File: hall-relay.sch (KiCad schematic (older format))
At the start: 10 parts, among them J1 Screw_Terminal_1x04, Q1 AO3400, U1 HT71xx, U2 Hall-A3212

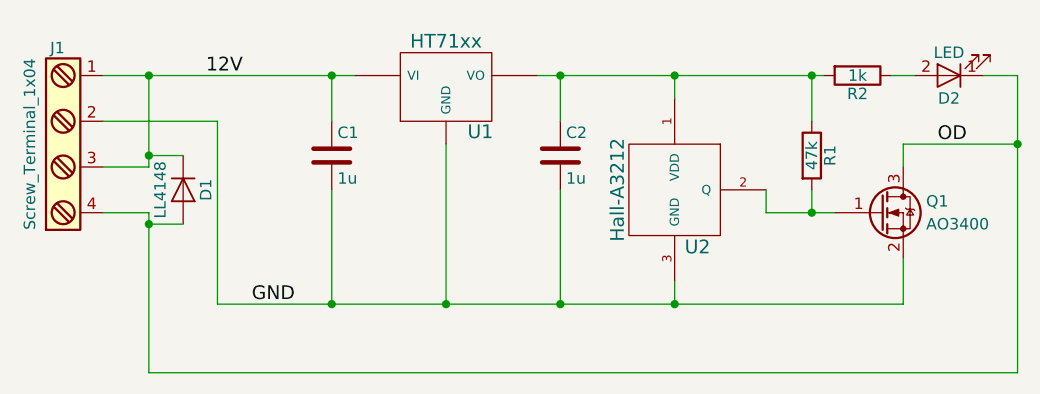
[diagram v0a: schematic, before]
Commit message: added LED pullup option to unregulated; avoids LED reverse-breakdown problems
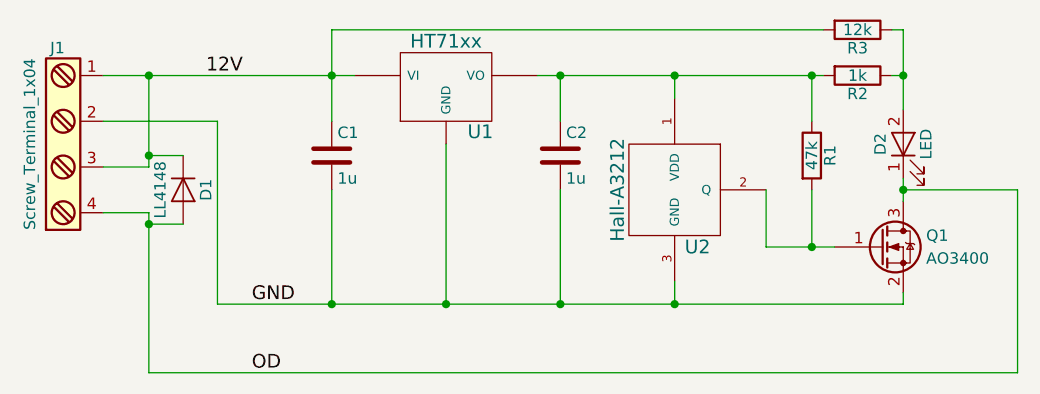
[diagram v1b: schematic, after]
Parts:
- added R3: 12k, Resistors_SMD:R_0805, symbol R
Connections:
- net 12V: now also R3.2
- net at D2.2 (A), R2.1: now also R3.1
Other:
- moved on the sheet: D2, Q1
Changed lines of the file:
@@
 	0    1    1    0
 $EndComp
-Text Label 6650 2200 0    60   ~ 0
-OD
 $Comp
 L Hall-A3212 U2
@@
 L Q_NMOS_GSD Q1
 U 1 1 5A364DBD
-P 6400 2500
-F 0 "Q1" H 6600 2550 50  0000 L CNN
-F 1 "AO3400" H 6600 2450 50  0000 L CNN
-F 2 "TO_SOT_Packages_SMD:SOT-23" H 6600 2600 50  0001 C CNN
-F 3 "" H 6400 2500 50  0000 C CNN
-	1    6400 2500
+P 6400 2650
+F 0 "Q1" H 6600 2700 50  0000 L CNN
+F 1 "AO3400" H 6600 2600 50  0000 L CNN
+F 2 "TO_SOT_Packages_SMD:SOT-23" H 6600 2750 50  0001 C CNN
+F 3 "" H 6400 2650 50  0000 C CNN
+	1    6400 2650
 	1    0    0    -1
 $EndComp
@@
 L LED D2
 U 1 1 5A366503
-P 6700 1900
-F 0 "D2" H 6700 2000 50  0000 C CNN
-F 1 "LED" H 6700 1800 50  0000 C CNN
-F 2 "LEDs:LED_0805" H 6700 1900 50  0001 C CNN
-F 3 "" H 6700 1900 50  0000 C CNN
-	1    6700 1900
-	-1   0    0    1
+P 6500 2200
+F 0 "D2" H 6500 2300 50  0000 C CNN
+F 1 "LED" H 6500 2100 50  0000 C CNN
+F 2 "LEDs:LED_0805" H 6500 2200 50  0001 C CNN
+F 3 "" H 6500 2200 50  0000 C CNN
+	1    6500 2200
+	0    -1   -1   0
 $EndComp
 $Comp
@@
 	3500 2100 3500 2900
 Wire Wire Line
-	6500 2900 6500 2700
-Wire Wire Line
 	4000 2400 4000 2900
 Connection ~ 4000 2900
@@
 	3200 2300 3200 1900
 Connection ~ 3200 1900
-Wire Wire Line
-	6500 2200 7000 2200
-Wire Wire Line
-	7000 1900 7000 3200
 Wire Wire Line
 	7000 3200 3200 3200
@@
 Connection ~ 5000 1900
 Wire Wire Line
-	6100 2400 6100 2500
-Wire Wire Line
-	5900 2500 6200 2500
+	6100 2400 6100 2650
 Wire Wire Line
 	5500 1900 5500 2000
 Connection ~ 5500 1900
 Wire Wire Line
-	5900 2400 5900 2500
-Connection ~ 6100 2500
+	5900 2400 5900 2650
 Wire Wire Line
 	5500 2800 5500 2900
@@
 	3500 2900 6500 2900
 Connection ~ 6100 1900
-Connection ~ 7000 2200
 Wire Wire Line
 	3200 2250 3350 2250
@@
 Connection ~ 3200 2550
 Wire Wire Line
-	4000 1900 4000 2100
-Wire Wire Line
-	6500 2200 6500 2300
+	4000 1700 4000 2100
 Wire Wire Line
 	6100 2100 6100 1900
+$Comp
+L R R3
+U 1 1 5A37822D
+P 6300 1700
+F 0 "R3" V 6380 1700 50  0000 C CNN
+F 1 "12k" V 6300 1700 50  0000 C CNN
+F 2 "Resistors_SMD:R_0805" V 6230 1700 50  0001 C CNN
+F 3 "" H 6300 1700 50  0000 C CNN
+	1    6300 1700
+	0    1    1    0
+$EndComp
 Wire Wire Line
-	6450 1900 6550 1900
+	6450 1700 6500 1700
 Wire Wire Line
-	6850 1900 7000 1900
+	6500 1700 6500 2050
+Connection ~ 6500 1900
+Wire Wire Line
+	6150 1700 4000 1700
+Text Label 3650 3200 0    60   ~ 0
+OD
+Wire Wire Line
+	5900 2650 6200 2650
+Connection ~ 6100 2650
+Wire Wire Line
+	6500 2900 6500 2850
+Wire Wire Line
+	6500 2450 6500 2350
+Wire Wire Line
+	7000 3200 7000 2400
+Wire Wire Line
+	7000 2400 6500 2400
+Connection ~ 6500 2400
+Wire Wire Line
+	6450 1900 6500 1900
 $EndSCHEMATC
